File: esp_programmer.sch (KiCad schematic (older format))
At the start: 6 parts, among them IC1 ESP8266_IN-LINE

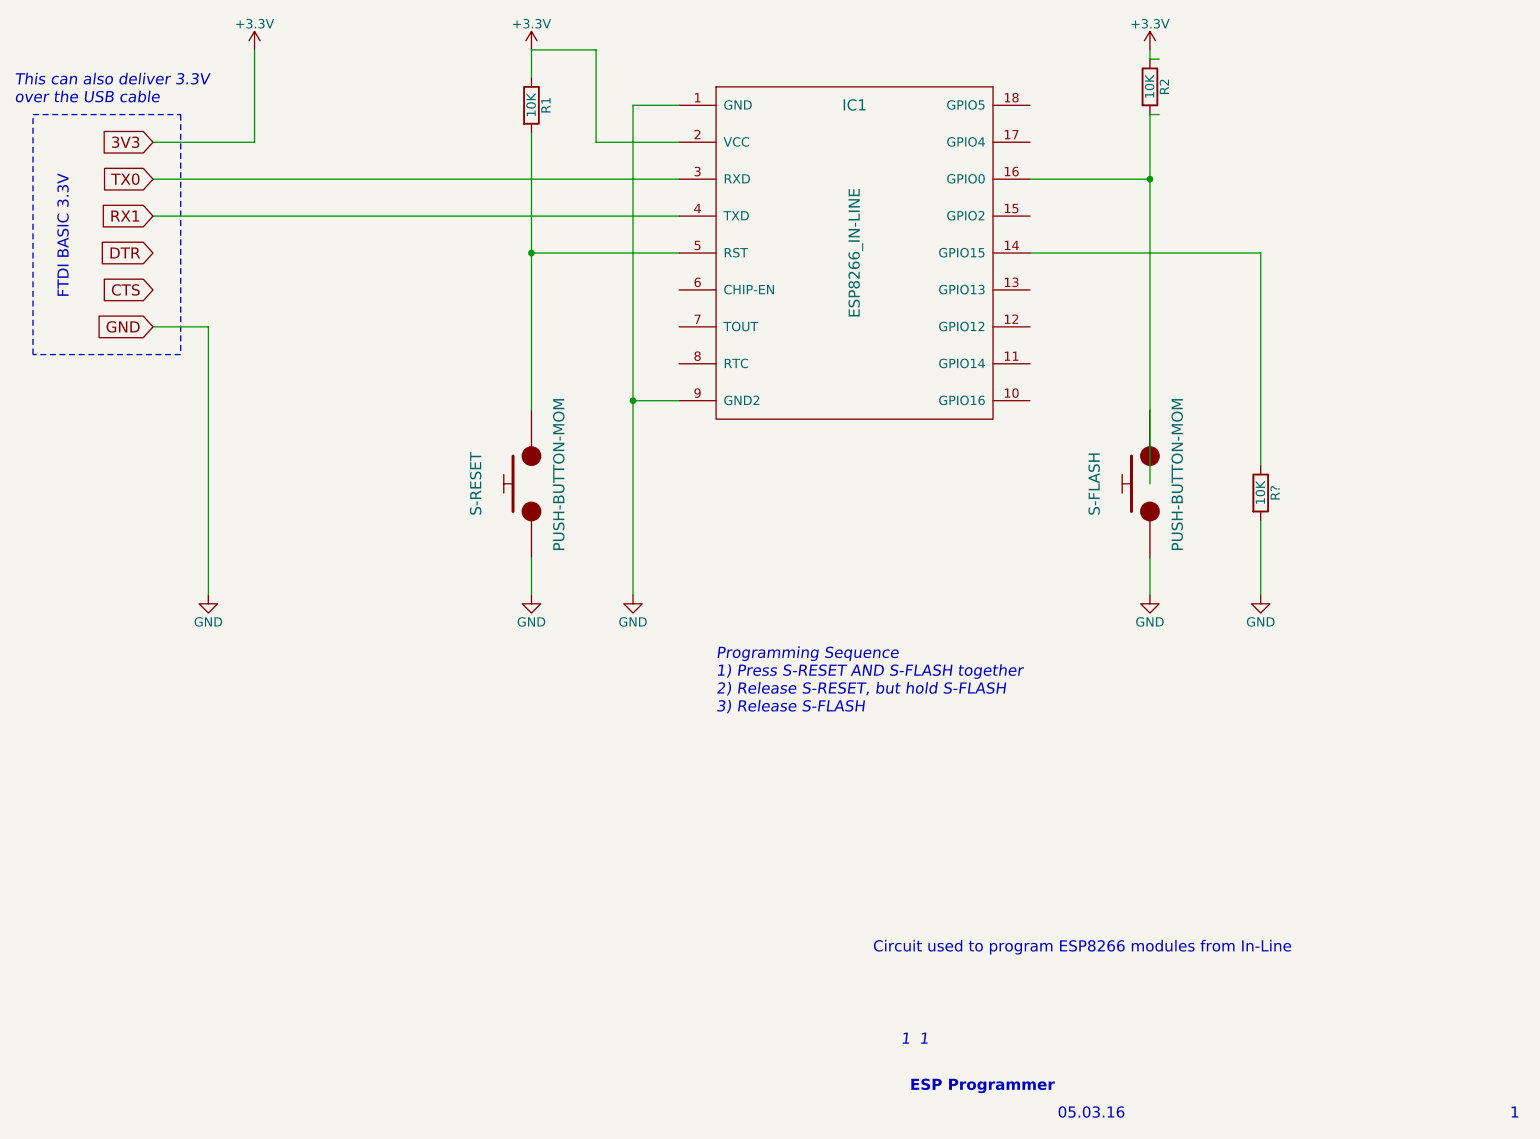
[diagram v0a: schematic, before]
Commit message: Tidied up schematic
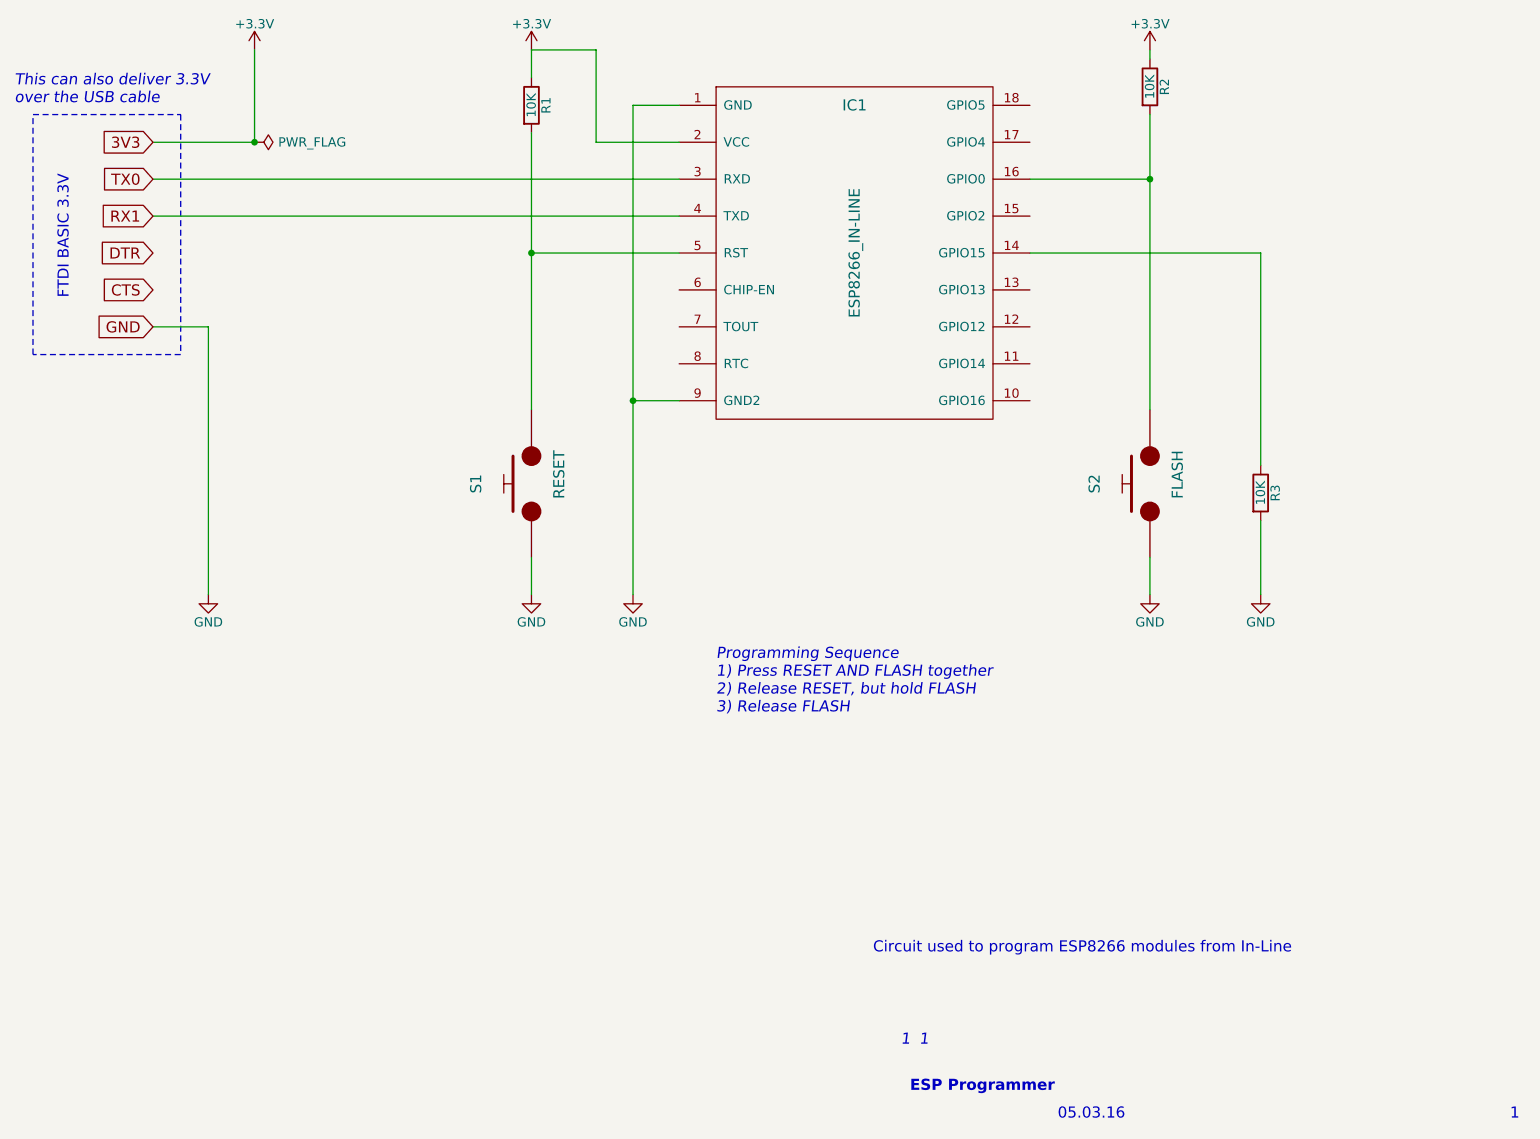
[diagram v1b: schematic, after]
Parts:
- S1: renamed from S-RESET; value PUSH-BUTTON-MOM -> RESET
- S2: renamed from S-FLASH; value PUSH-BUTTON-MOM -> FLASH
- gave numbers to parts that had none: 1
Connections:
- wire segments 28 -> 26
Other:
- note added: "Programming Sequence\n1) Press RESET AND FLASH together\n2) Release RESET, but hold FLASH\n3) Release FLASH"
- note removed: "Programming Sequence\n1) Press S-RESET AND S-FLASH together\n2) Release S-RESET, but hold S-FLASH\n3) Release S-FLASH"
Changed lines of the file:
@@
 DTR
 $Comp
-L power:+3.3V #PWR?
+L power:+3.3V #PWR0101
 U 1 1 56BF1C8B
 P 3800 1850
-F 0 "#PWR?" H 3800 1700 50  0001 C CNN
+F 0 "#PWR0101" H 3800 1700 50  0001 C CNN
 F 1 "+3.3V" H 3800 1990 50  0000 C CNN
 F 2 "" H 3800 1850 50  0000 C CNN
@@
 $EndComp
 $Comp
-L power:+3.3V #PWR?
+L power:+3.3V #PWR0102
 U 1 1 56BF1C9F
 P 5300 1850
-F 0 "#PWR?" H 5300 1700 50  0001 C CNN
+F 0 "#PWR0102" H 5300 1700 50  0001 C CNN
 F 1 "+3.3V" H 5300 1990 50  0000 C CNN
 F 2 "" H 5300 1850 50  0000 C CNN
@@
 $EndComp
 $Comp
-L power:GND #PWR?
+L power:GND #PWR0103
 U 1 1 56BF1CC2
 P 3550 4800
-F 0 "#PWR?" H 3550 4550 50  0001 C CNN
+F 0 "#PWR0103" H 3550 4550 50  0001 C CNN
 F 1 "GND" H 3550 4650 50  0000 C CNN
 F 2 "" H 3550 4800 50  0000 C CNN
@@
 $EndComp
 $Comp
-L power:GND #PWR?
+L power:GND #PWR0104
 U 1 1 56BF1CD6
 P 5300 4800
-F 0 "#PWR?" H 5300 4550 50  0001 C CNN
+F 0 "#PWR0104" H 5300 4550 50  0001 C CNN
 F 1 "GND" H 5300 4650 50  0000 C CNN
 F 2 "" H 5300 4800 50  0000 C CNN
@@
 	1    0    0    -1
 $EndComp
-$Comp
-L esp_programmer-rescue:PUSH-BUTTON-MOM S-FLASH
-U 1 1 56BF3AFC
-P 8650 4200
-F 0 "S-FLASH" H 8650 4500 60  0000 C CNN
-F 1 "PUSH-BUTTON-MOM" H 8700 4050 60  0000 C CNN
-F 2 "" H 8650 4200 60  0000 C CNN
-F 3 "" H 8650 4200 60  0000 C CNN
-	1    8650 4200
-	0    -1   -1   0
-$EndComp
-$Comp
-L esp_programmer-rescue:PUSH-BUTTON-MOM S-RESET
-U 1 1 56BF3B59
-P 5300 4200
-F 0 "S-RESET" H 5300 4500 60  0000 C CNN
-F 1 "PUSH-BUTTON-MOM" H 5350 4050 60  0000 C CNN
-F 2 "" H 5300 4200 60  0000 C CNN
-F 3 "" H 5300 4200 60  0000 C CNN
-	1    5300 4200
-	0    -1   -1   0
-$EndComp
 Wire Wire Line
 	3250 2350 3800 2350
@@
 Wire Wire Line
 	5300 2000 5300 1850
-Wire Wire Line
-	8000 2550 8650 2550
-Wire Wire Line
-	8650 2200 8650 2550
 $Comp
 L Device:R R2
@@
 	1    0    0    -1
 $EndComp
-Wire Wire Line
-	8650 2200 8700 2200
-Connection ~ 8650 2550
-$Comp
-L power:+3.3V #PWR?
+$Comp
+L power:+3.3V #PWR0105
 U 1 1 56BF4640
 P 8650 1850
-F 0 "#PWR?" H 8650 1700 50  0001 C CNN
+F 0 "#PWR0105" H 8650 1700 50  0001 C CNN
 F 1 "+3.3V" H 8650 1990 50  0000 C CNN
 F 2 "" H 8650 1850 50  0000 C CNN
@@
 $EndComp
 Wire Wire Line
-	8700 1900 8650 1900
-Wire Wire Line
 	8650 1900 8650 1850
 $Comp
-L power:GND #PWR?
+L power:GND #PWR0106
 U 1 1 56BF4BBA
 P 8650 4800
-F 0 "#PWR?" H 8650 4550 50  0001 C CNN
+F 0 "#PWR0106" H 8650 4550 50  0001 C CNN
 F 1 "GND" H 8650 4650 50  0000 C CNN
 F 2 "" H 8650 4800 50  0000 C CNN
@@
 $EndComp
 $Comp
-L power:GND #PWR?
+L power:GND #PWR0107
 U 1 1 56BF4BF3
 P 5850 4800
-F 0 "#PWR?" H 5850 4550 50  0001 C CNN
+F 0 "#PWR0107" H 5850 4550 50  0001 C CNN
 F 1 "GND" H 5850 4650 50  0000 C CNN
 F 2 "" H 5850 4800 50  0000 C CNN
@@
 	6100 3750 5850 3750
 Connection ~ 5850 3750
-Wire Wire Line
-	8650 4600 8650 4800
 Wire Wire Line
 	5300 4600 5300 4800
@@
 1
 Text Notes 6300 5450 0    60   Italic 0
-Programming Sequence\n1) Press S-RESET AND S-FLASH together\n2) Release S-RESET, but hold S-FLASH\n3) Release S-FLASH
+Programming Sequence\n1) Press RESET AND FLASH together\n2) Release RESET, but hold FLASH\n3) Release FLASH
 Text Notes 7150 6750 0    60   ~ 0
 Circuit used to program ESP8266 modules from In-Line
@@
 This can also deliver 3.3V \nover the USB cable
 $Comp
-L Device:R R?
+L Device:R R3
 U 1 1 56DB17D5
 P 9250 4250
-F 0 "R?" V 9330 4250 50  0000 C CNN
+F 0 "R3" V 9330 4250 50  0000 C CNN
 F 1 "10K" V 9250 4250 50  0000 C CNN
 F 2 "" V 9180 4250 50  0000 C CNN
@@
 	9250 2950 9250 4100
 $Comp
-L power:GND #PWR?
+L power:GND #PWR0108
 U 1 1 56DB191E
 P 9250 4800
-F 0 "#PWR?" H 9250 4550 50  0001 C CNN
+F 0 "#PWR0108" H 9250 4550 50  0001 C CNN
 F 1 "GND" H 9250 4650 50  0000 C CNN
 F 2 "" H 9250 4800 50  0000 C CNN
@@
 	5300 2950 5300 3800
 Wire Wire Line
-	8650 2550 8650 4200
-Wire Wire Line
 	5850 3750 5850 4800
+$Comp
+L esp_programmer-rescue:PUSH-BUTTON-MOM S1
+U 1 1 56BF3B59
+P 5300 4200
+F 0 "S1" H 5300 4500 60  0000 C CNN
+F 1 "RESET" H 5350 4050 60  0000 C CNN
+F 2 "" H 5300 4200 60  0000 C CNN
+F 3 "" H 5300 4200 60  0000 C CNN
+	1    5300 4200
+	0    -1   -1   0
+$EndComp
+$Comp
+L power:PWR_FLAG #FLG0101
+U 1 1 61F54E3E
+P 3800 2350
+F 0 "#FLG0101" H 3800 2425 50  0001 C CNN
+F 1 "PWR_FLAG" V 3800 2478 50  0000 L CNN
+F 2 "" H 3800 2350 50  0001 C CNN
+F 3 "~" H 3800 2350 50  0001 C CNN
+	1    3800 2350
+	0    1    1    0
+$EndComp
+Connection ~ 3800 2350
+Wire Wire Line
+	8650 4600 8650 4800
+$Comp
+L esp_programmer-rescue:PUSH-BUTTON-MOM S2
+U 1 1 56BF3AFC
+P 8650 4200
+F 0 "S2" H 8650 4500 60  0000 C CNN
+F 1 "FLASH" H 8700 4050 60  0000 C CNN
+F 2 "" H 8650 4200 60  0000 C CNN
+F 3 "" H 8650 4200 60  0000 C CNN
+	1    8650 4200
+	0    -1   -1   0
+$EndComp
+Wire Wire Line
+	8650 2200 8650 2550
+Wire Wire Line
+	8000 2550 8650 2550
+Wire Wire Line
+	8650 2550 8650 3800
+Connection ~ 8650 2550
 $EndSCHEMATC
